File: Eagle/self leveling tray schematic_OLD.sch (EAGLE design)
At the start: 19 parts

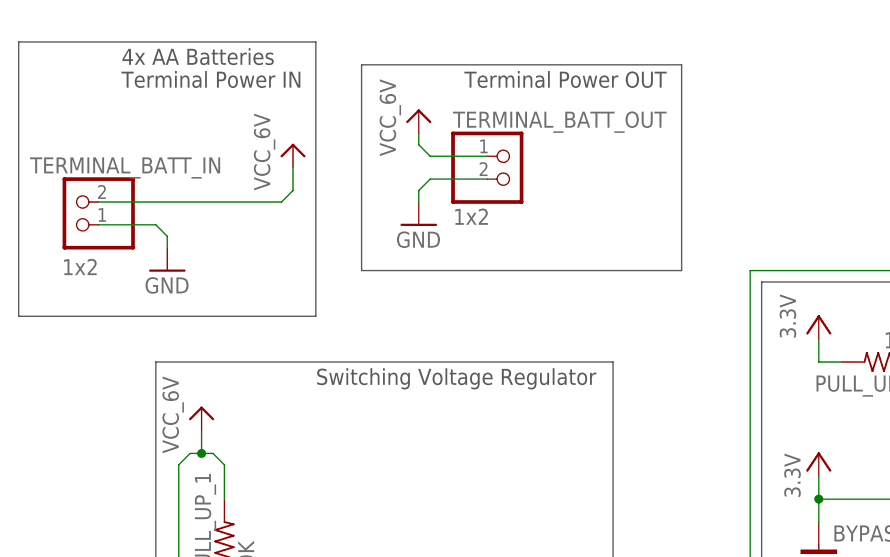
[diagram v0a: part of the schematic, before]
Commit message: Schematic Updates
Updated with better supply layout and more organization.
Also changed filename to have team name.
Still Need: Oscillator, LEDs, UART review
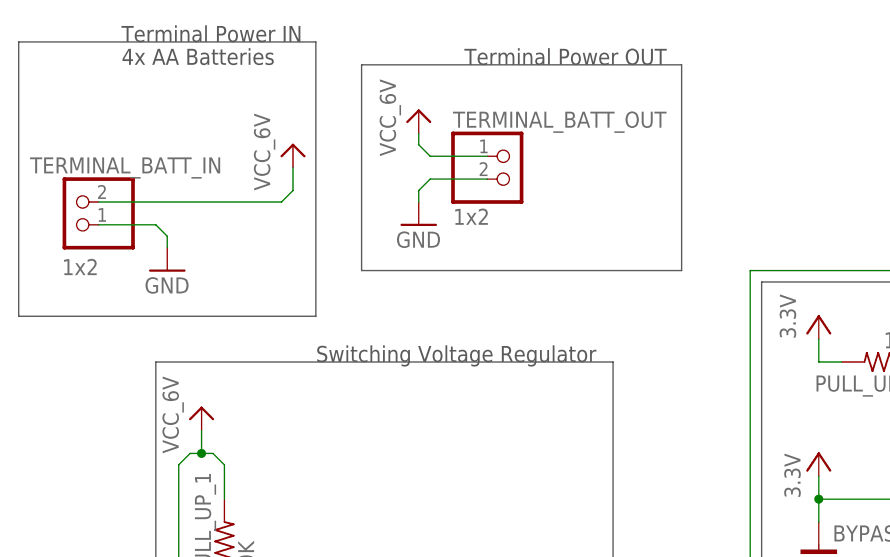
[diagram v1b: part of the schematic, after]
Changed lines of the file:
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@@
 <wire x1="152.4" y1="52.07" x2="77.47" y2="52.07" width="0.1524" layer="97"/>
 <wire x1="77.47" y1="52.07" x2="77.47" y2="130.81" width="0.1524" layer="97"/>
-<text x="6.35" y="152.4" size="1.778" layer="97">Terminal Power IN</text>
-<text x="44.45" y="152.4" size="1.778" layer="97">Terminal Power OUT</text>
-<text x="27.94" y="119.38" size="1.778" layer="97">Switching Voltage Regulator</text>
+<text x="6.35" y="157.48" size="1.778" layer="97">Terminal Power IN</text>
+<text x="44.45" y="154.94" size="1.778" layer="97">Terminal Power OUT</text>
+<text x="27.94" y="121.92" size="1.778" layer="97">Switching Voltage Regulator</text>
 </plain>
 <instances>
